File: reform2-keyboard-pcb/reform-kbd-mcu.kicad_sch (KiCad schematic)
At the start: 32 parts, among them J1 USB, J2 UART, J3 AUX, J4 Desktop USB, J6 AUX, SW83 RESET, SW84 SW_DIP_x01, U1 ATMEGA32U4-AU, U3 MCP1700-3302E_SOT23, Y1 16MHz

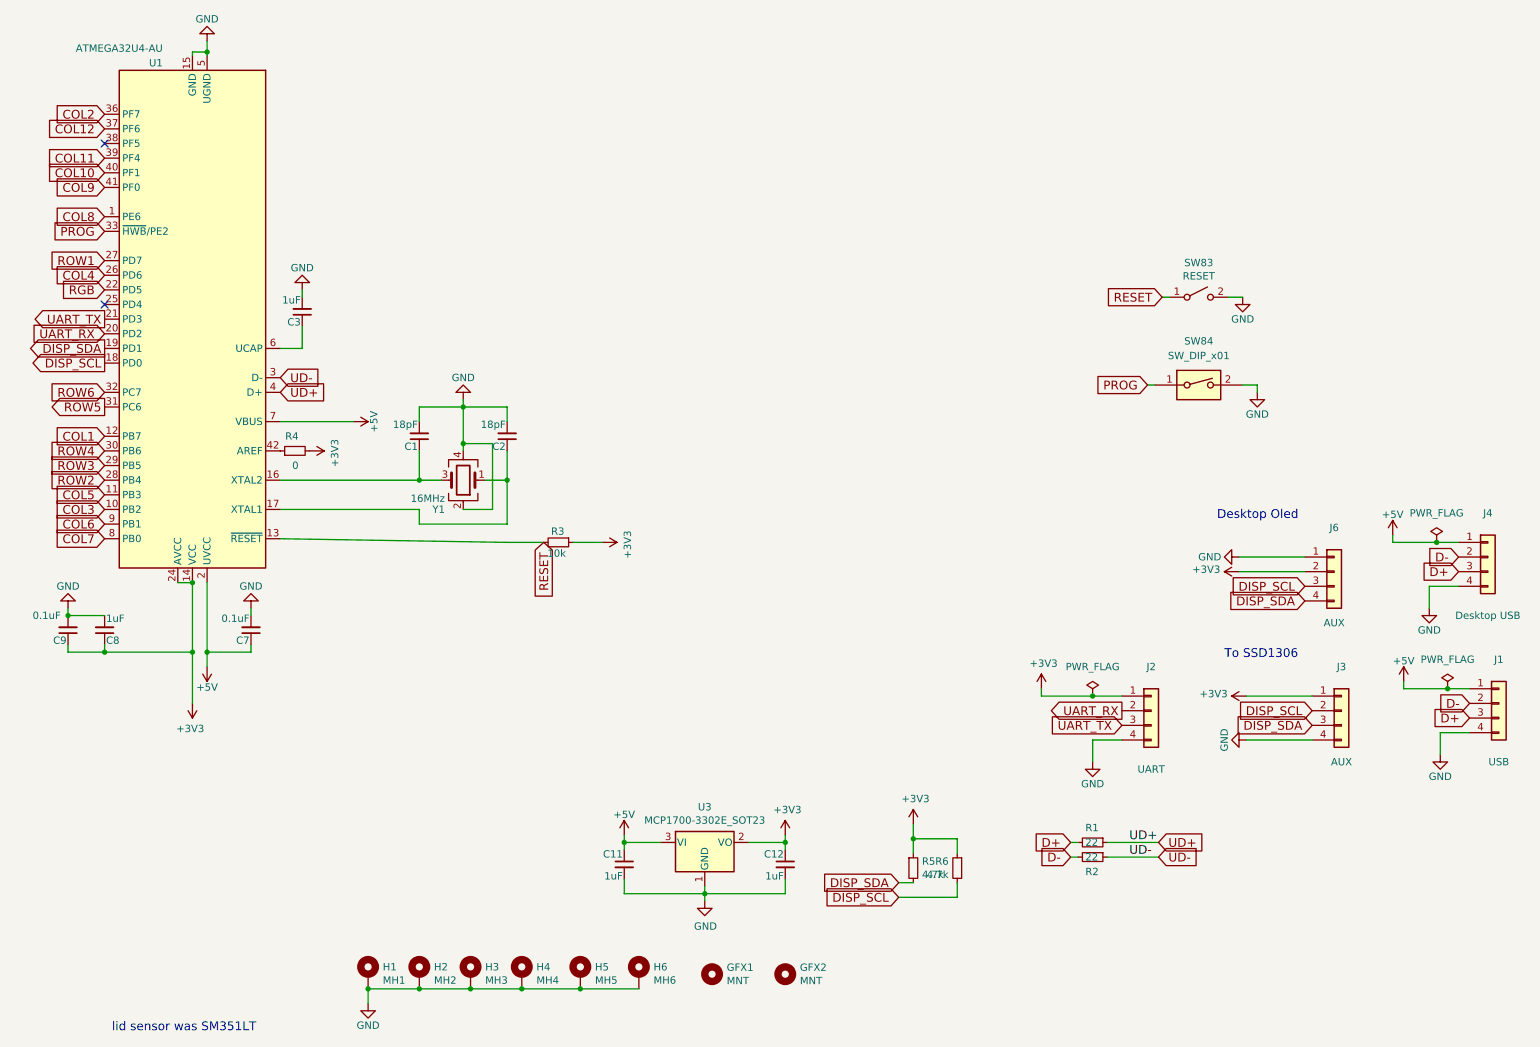
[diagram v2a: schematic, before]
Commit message: teensy2 w/ external 3volt regulator
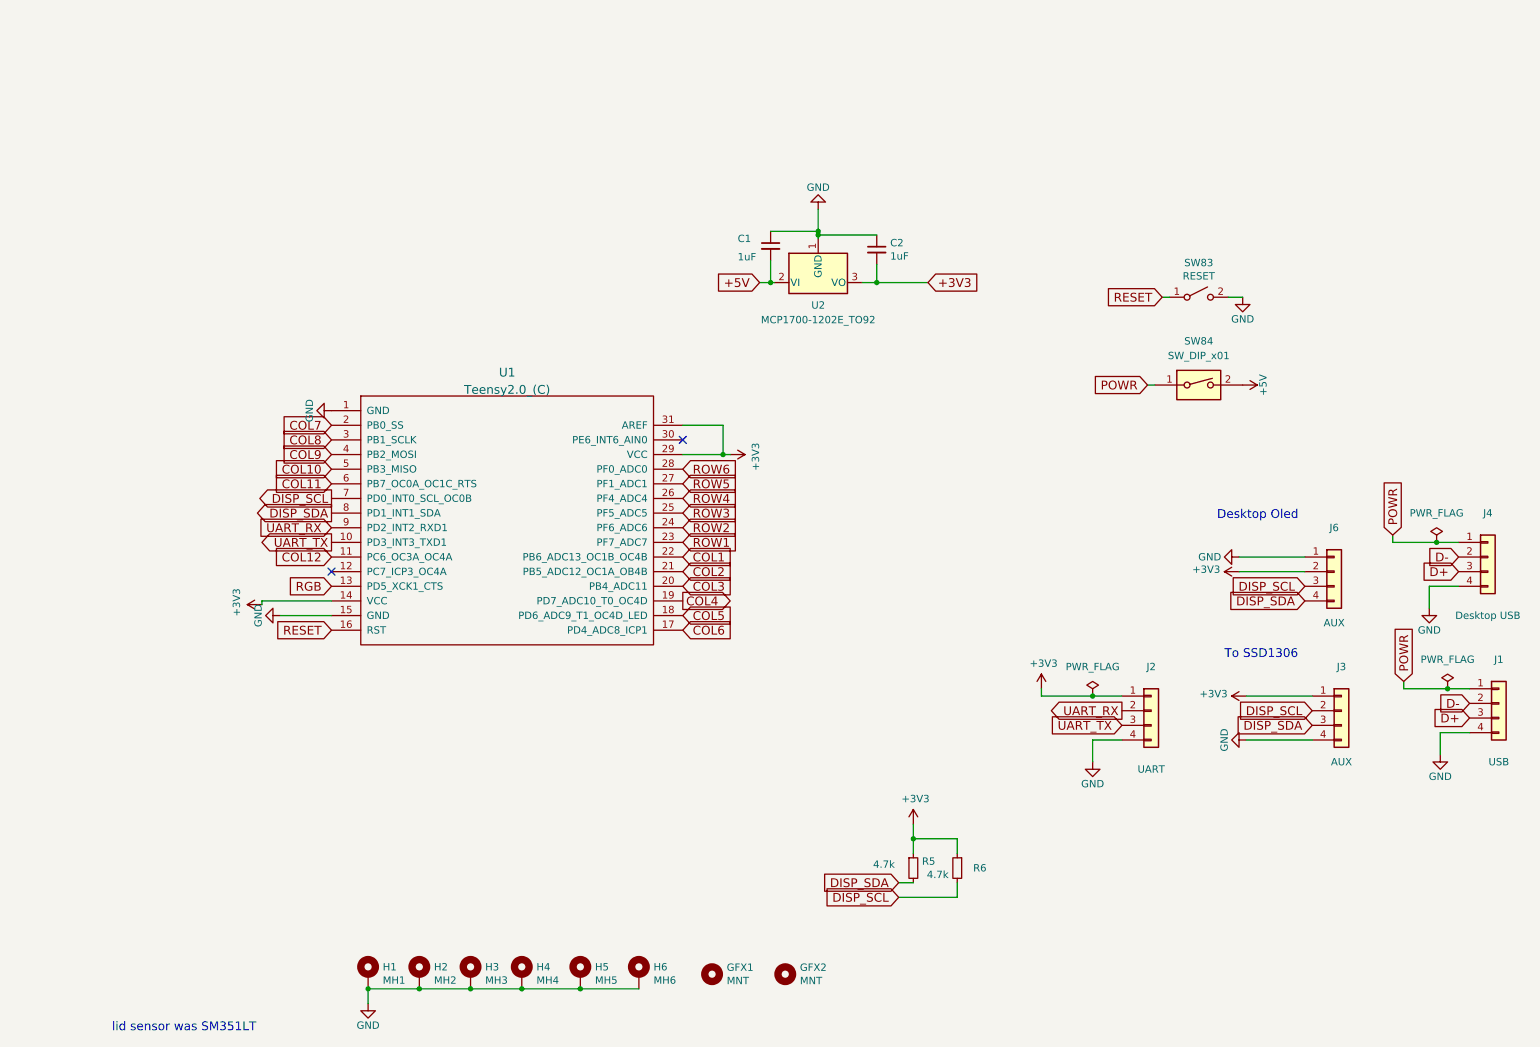
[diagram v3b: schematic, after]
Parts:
- removed C11, C12, C3, C8: 1uF, Capacitor_SMD:C_0805_2012Metric_Pad1.18x1.45mm_HandSolder, symbol reform2-keyboard-rescue:C_Small-Device
- removed C7, C9: 0.1uF, Capacitor_SMD:C_0805_2012Metric_Pad1.18x1.45mm_HandSolder, symbol reform2-keyboard-rescue:C_Small-Device
- removed R1, R2: 22, Resistor_SMD:R_0805_2012Metric_Pad1.20x1.40mm_HandSolder, symbol reform2-keyboard-rescue:R_Small-Device
- removed R3: 10k, Resistor_SMD:R_0805_2012Metric_Pad1.20x1.40mm_HandSolder, symbol reform2-keyboard-rescue:R_Small-Device
- removed R4: 0, Resistor_SMD:R_0805_2012Metric_Pad1.20x1.40mm_HandSolder, symbol reform2-keyboard-rescue:R_Small-Device
- removed U1: ATMEGA32U4-AU, Package_QFP:TQFP-44_10x10mm_P0.8mm, symbol reform2-keyboard-rescue:ATmega32U4-AU-MCU_Microchip_ATmega
- removed U3: MCP1700-3302E_SOT23, Package_TO_SOT_SMD:SOT-23, symbol reform2-keyboard-rescue:MCP1700-3302E_SOT23-Regulator_Linear
- removed Y1: 16MHz, Crystal:Crystal_SMD_3225-4Pin_3.2x2.5mm_HandSoldering, symbol reform2-keyboard-rescue:Crystal_GND24-Device
- added U1: Teensy2.0_(C), teensy:Teensy2.0, symbol teensy:Teensy2.0_(C)
- added U2: MCP1700-1202E_TO92, Package_TO_SOT_THT:TO-92_Inline, symbol Regulator_Linear:MCP1700-1202E_TO92
- C1, C2: value 18pF -> 1uF; Manufacturer Yageo -> Taiyo Yuden; Manufacturer_No CC0603JRNPO9BN180 -> JMK107BB7475KA-T
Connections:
- net +3V3: now also C2.2, U1.14 (VCC), U1.29 (VCC), U1.31 (AREF), U2.3 (VO)
- net +5V: now also C1.2, SW84.2, U2.2 (VI); no longer J1.1 (Pin_1), J4.1 (Pin_1)
- net COL1: now also U1.22 (PB6_ADC13_OC1B_OC4B)
- net COL10: now also U1.5 (PB3_MISO)
- net COL11: now also U1.6 (PB7_OC0A_OC1C_RTS)
- net COL12: now also U1.11 (PC6_OC3A_OC4A)
- net COL2: now also U1.21 (PB5_ADC12_OC1A_OB4B)
- net COL3: now also U1.20 (PB4_ADC11)
- net COL4: now also U1.19 (PD7_ADC10_T0_OC4D)
- net COL5: now also U1.18 (PD6_ADC9_T1_OC4D_LED)
- net COL6: now also U1.17 (PD4_ADC8_ICP1)
- net COL7: now also U1.2 (PB0_SS)
- net COL8: now also U1.3 (PB1_SCLK)
- net COL9: now also U1.4 (PB2_MOSI)
- net DISP_SCL: now also U1.7 (PD0_INT0_SCL_OC0B)
- net DISP_SDA: now also U1.8 (PD1_INT1_SDA)
- net GND: now also C1.1, C2.1, U1.1 (GND), U1.15 (GND), U2.1 (GND); no longer C1.2, C2.2, SW84.2
- net RESET: now also U1.16 (RST)
- net RGB: now also U1.13 (PD5_XCK1_CTS)
- net ROW1: now also U1.23 (PF7_ADC7)
- net ROW2: now also U1.24 (PF6_ADC6)
- net ROW3: now also U1.25 (PF5_ADC5)
- net ROW4: now also U1.26 (PF4_ADC4)
- net ROW5: now also U1.27 (PF1_ADC1)
- net ROW6: now also U1.28 (PF0_ADC0)
- net UART_RX: now also U1.9 (PD2_INT2_RXD1)
- net UART_TX: now also U1.10 (PD3_INT3_TXD1)
- net PROG renamed POWR
- net POWR: now also J1.1 (Pin_1), J4.1 (Pin_1)

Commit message: initial itsybitsy. Moved USB airwire & lcd locations
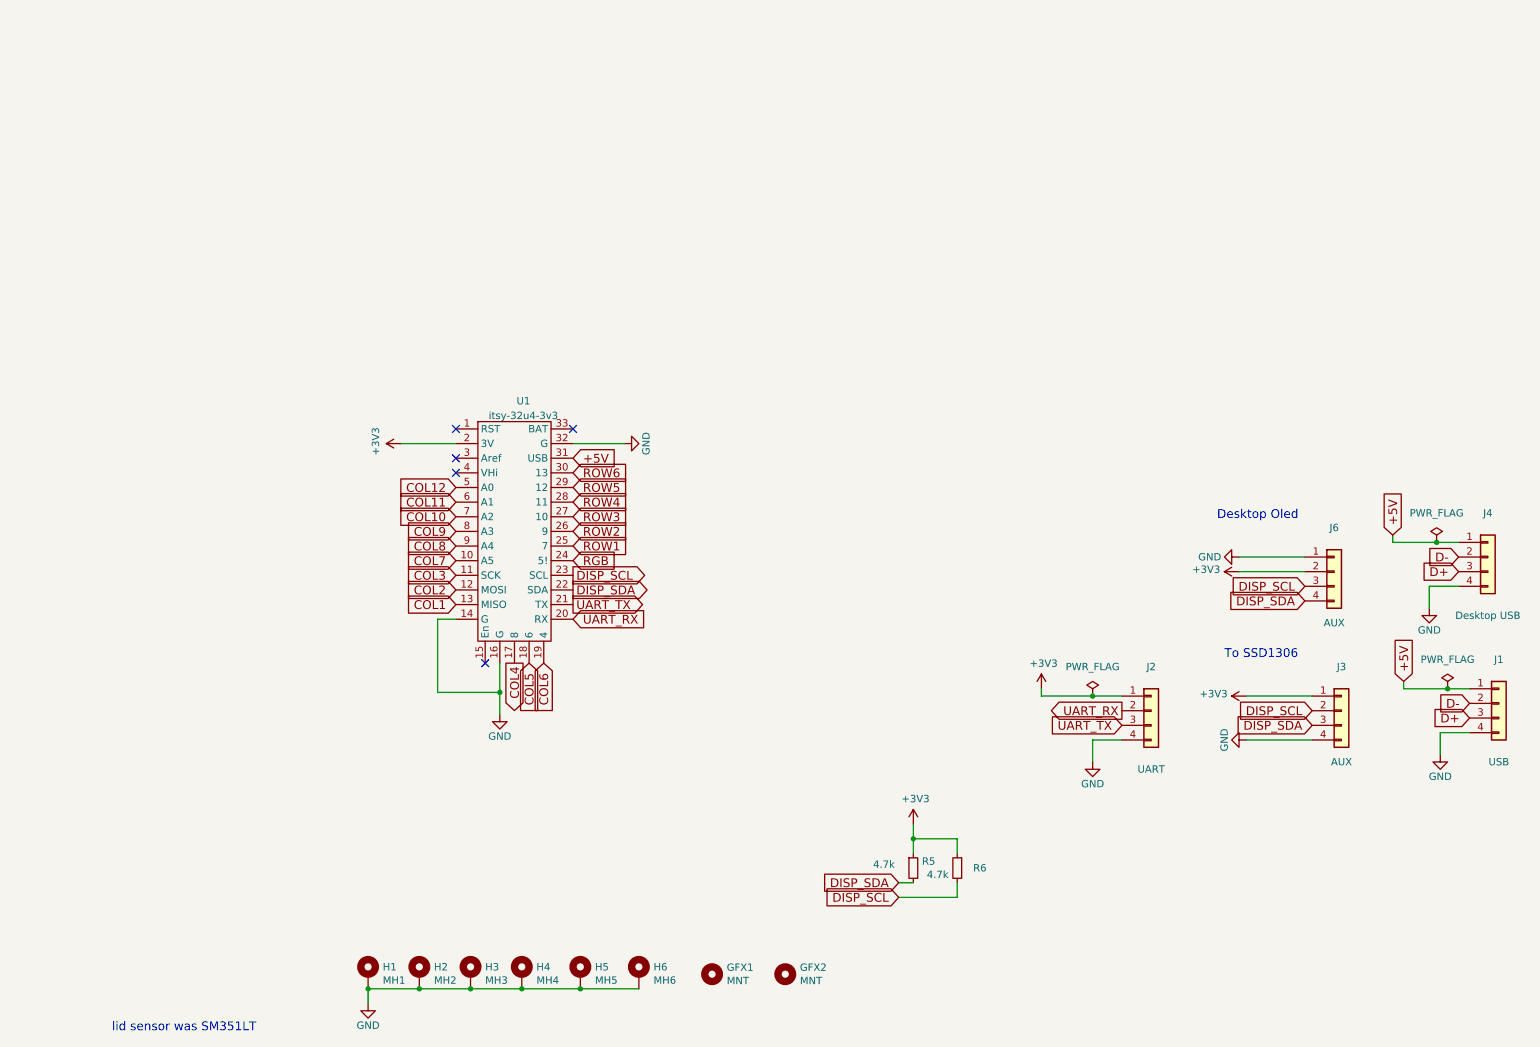
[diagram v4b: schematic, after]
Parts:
- removed C1, C2: 1uF, Capacitor_SMD:C_0805_2012Metric_Pad1.18x1.45mm_HandSolder, symbol reform2-keyboard-rescue:C_Small-Device
- removed SW83: RESET, Button_Switch_SMD:SW_Push_1P1T_NO_CK_KMR2, symbol reform2-keyboard-rescue:SW_SPST-Switch
- removed SW84: SW_DIP_x01, Button_Switch_SMD:SW_DIP_SPSTx01_Slide_Omron_A6S-110x_W8.9mm_P2.54mm, symbol reform2-keyboard-rescue:SW_DIP_x01-Switch
- removed U1: Teensy2.0_(C), teensy:Teensy2.0, symbol teensy:Teensy2.0_(C)
- removed U2: MCP1700-1202E_TO92, Package_TO_SOT_THT:TO-92_Inline, symbol Regulator_Linear:MCP1700-1202E_TO92
- added U1: itsy-32u4-3v3, Itsybitsy32u4:ItsyBitsy-32u4, symbol itsybitsy32u4:itsy-32u4-3v3
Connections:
- net POWR is gone; now on net +5V: J1.1 (Pin_1), J4.1 (Pin_1)
- net +3V3: now also U1.2 (3V)
- net +5V: now also U1.31 (USB)
- net COL1: now also U1.13 (MISO)
- net COL10: now also U1.7 (A2)
- net COL11: now also U1.6 (A1)
- net COL12: now also U1.5 (A0)
- net COL2: now also U1.12 (MOSI)
- net COL3: now also U1.11 (SCK)
- net COL4: now also U1.17 (8)
- net COL5: now also U1.18 (6)
- net COL6: now also U1.19 (4)
- net COL7: now also U1.10 (A5)
- net COL8: now also U1.9 (A4)
- net COL9: now also U1.8 (A3)
- net DISP_SCL: now also U1.23 (SCL)
- net DISP_SDA: now also U1.22 (SDA)
- net GND: now also U1.14 (G), U1.16 (G), U1.32 (G)
- net RGB: now also U1.24 (5!)
- net ROW1: now also U1.25 (7)
- net ROW2: now also U1.26 (9)
- net ROW3: now also U1.27 (10)
- net ROW4: now also U1.28 (11)
- net ROW5: now also U1.29 (12)
- net ROW6: now also U1.30 (13)
- net UART_RX: now also U1.20 (RX)
- net UART_TX: now also U1.21 (TX)
- no-connect marks 2 -> 5

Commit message: added testpoints for RGB, fixed diode directions, started BOM & top POS for assembly
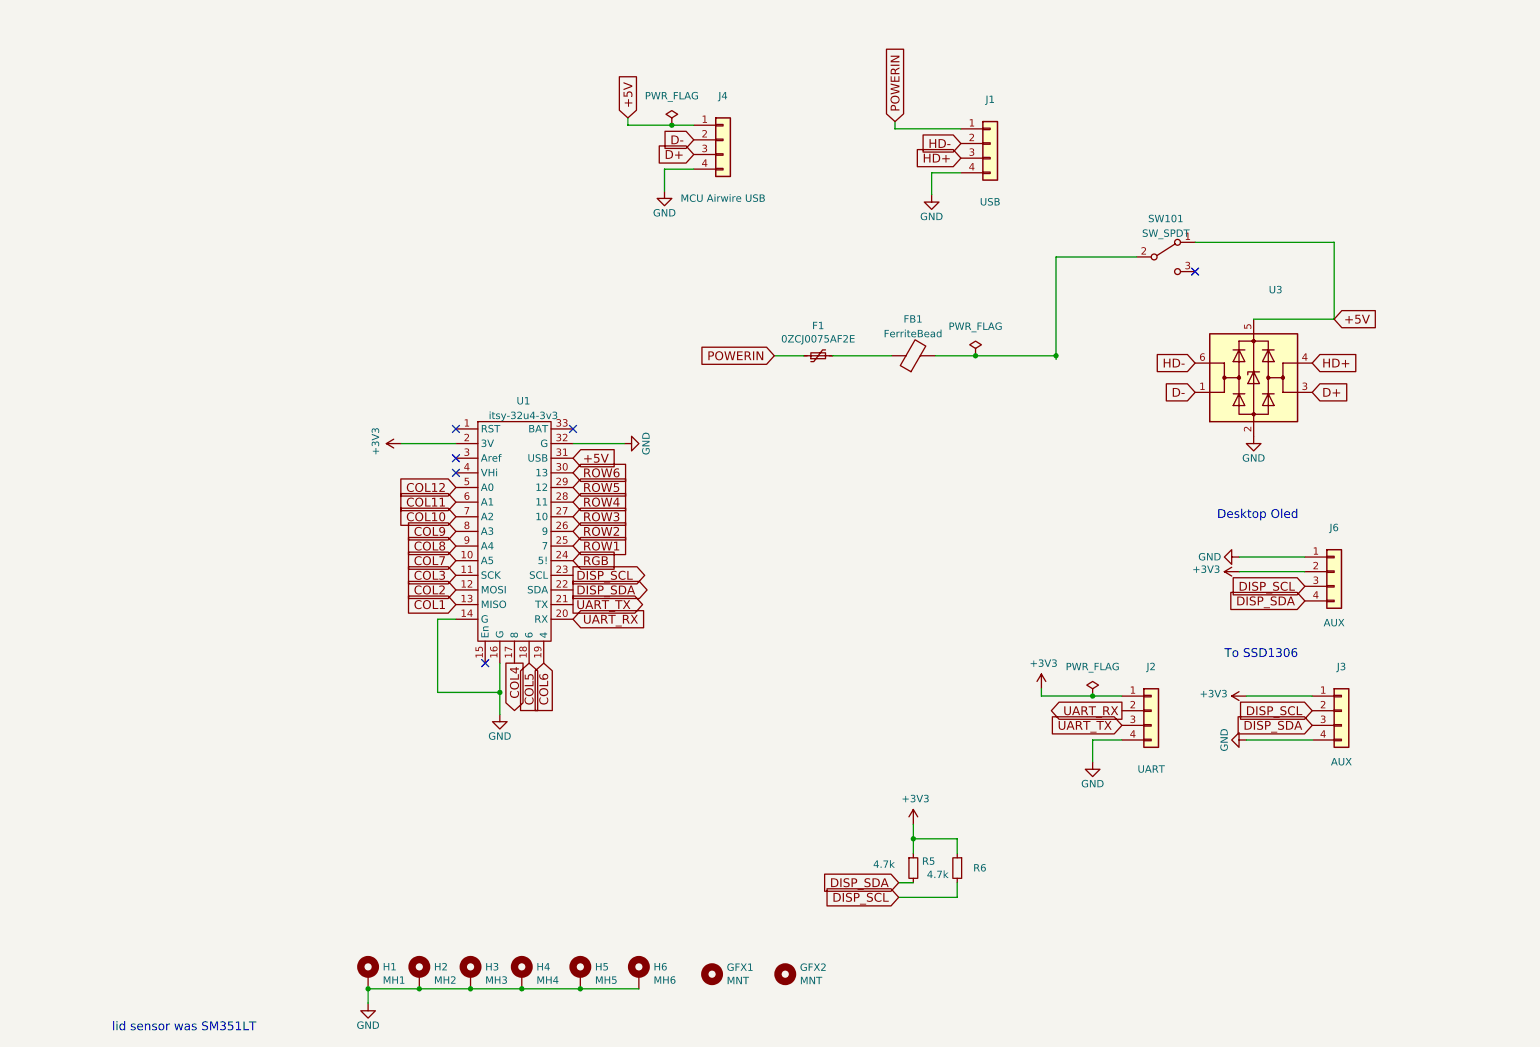
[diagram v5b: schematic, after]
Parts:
- added F1: 0ZCJ0075AF2E, Resistor_SMD:R_1206_3216Metric, symbol Device:Polyfuse_Small
- added FB1: FerriteBead, Resistor_SMD:R_0805_2012Metric_Pad1.20x1.40mm_HandSolder, symbol Device:FerriteBead
- added SW101: SW_SPDT, Button_Switch_THT:SW_Push_1P2T_Vertical_E-Switch_800UDP8P1A1M6, symbol Switch:SW_SPDT
- added U3: ~, Package_TO_SOT_SMD:SOT-23-6_Handsoldering, symbol Power_Protection:USBLC6-2SC6
- J4: value Desktop USB -> MCU Airwire USB; footprint Connector_PinHeader_2.54mm:PinHeader_1x04_P2.54mm_Horizontal -> Connector_PinHeader_2.54mm:PinHeader_1x04_P2.54mm_Vertical
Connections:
- net +5V: now also SW101.1 (A), U3.5 (VBUS); no longer J1.1 (Pin_1)
- net D+: now also U3.3 (I/O2); no longer J1.3 (Pin_3)
- net D-: now also U3.1 (I/O1); no longer J1.2 (Pin_2)
- net GND: now also U3.2 (GND)
- new net: FB1.2, SW101.2 (B)
- new net: F1.2, FB1.1
- new net HD+: J1.3 (Pin_3), U3.4 (I/O2)
- new net HD-: J1.2 (Pin_2), U3.6 (I/O1)
- new net POWERIN: F1.1, J1.1 (Pin_1)
- no-connect marks 5 -> 6
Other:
- moved on the sheet: J1, J4

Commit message: improve docs
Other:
- note added: "B1"
- note added: "B2"
- note added: "B3"
- note added: "B4"
- note added: "B5"
- note added: "B6"
- note added: "B7"
- note added: "C7"
- note added: "D0"
- note added: "D1"
- note added: "D2"
- note added: "D3"
- note added: "D4"
- note added: "D6"
- note added: "D7"
- note added: "E6"
- note added: "F0"
- note added: "F1"
- note added: "F4"
- note added: "F5"
- note added: "F6"
- note added: "F7"
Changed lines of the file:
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@@
     (stroke (width 0) (type default) (color 0 0 0 0))
   )
+  (text "B4" (at 96.52 140.335 90)
+    (effects (font (size 1.524 1.524)) (justify left bottom))
+  )
+  (text "D6" (at 116.205 96.52 0)
+    (effects (font (size 1.524 1.524)) (justify left bottom))
+  )
+  (text "F1" (at 70.485 107.315 0)
+    (effects (font (size 1.524 1.524)) (justify left bottom))
+  )
+  (text "E6" (at 114.935 107.315 0)
+    (effects (font (size 1.524 1.524)) (justify left bottom))
+  )
+  (text "B7" (at 115.57 99.695 0)
+    (effects (font (size 1.524 1.524)) (justify left bottom))
+  )
+  (text "D3" (at 119.38 117.475 0)
+    (effects (font (size 1.524 1.524)) (justify left bottom))
+  )
+  (text "C7" (at 114.935 109.855 0)
+    (effects (font (size 1.524 1.524)) (justify left bottom))
+  )
+  (text "D0" (at 120.015 111.76 0)
+    (effects (font (size 1.524 1.524)) (justify left bottom))
+  )
+  (text "B5" (at 114.935 104.775 0)
+    (effects (font (size 1.524 1.524)) (justify left bottom))
+  )
+  (text "F5" (at 70.485 102.235 0)
+    (effects (font (size 1.524 1.524)) (justify left bottom))
+  )
   (text "To SSD1306" (at 218.44 125.73 0)
+    (effects (font (size 1.524 1.524)) (justify left bottom))
+  )
+  (text "F6" (at 70.485 99.695 0)
+    (effects (font (size 1.524 1.524)) (justify left bottom))
+  )
+  (text "D7" (at 99.06 140.335 90)
+    (effects (font (size 1.524 1.524)) (justify left bottom))
+  )
+  (text "F0" (at 70.485 109.855 0)
+    (effects (font (size 1.524 1.524)) (justify left bottom))
+  )
+  (text "F7" (at 70.485 97.155 0)
+    (effects (font (size 1.524 1.524)) (justify left bottom))
+  )
+  (text "C7" (at 116.205 93.98 0)
+    (effects (font (size 1.524 1.524)) (justify left bottom))
+  )
+  (text "F4" (at 70.485 104.775 0)
+    (effects (font (size 1.524 1.524)) (justify left bottom))
+  )
+  (text "B2" (at 70.485 114.935 0)
+    (effects (font (size 1.524 1.524)) (justify left bottom))
+  )
+  (text "B6" (at 115.57 102.235 0)
     (effects (font (size 1.524 1.524)) (justify left bottom))
   )
@@
     (effects (font (size 1.524 1.524)) (justify left bottom))
   )
+  (text "B1" (at 70.485 112.395 0)
+    (effects (font (size 1.524 1.524)) (justify left bottom))
+  )
+  (text "D2" (at 119.38 120.015 0)
+    (effects (font (size 1.524 1.524)) (justify left bottom))
+  )
+  (text "B3" (at 70.485 117.475 0)
+    (effects (font (size 1.524 1.524)) (justify left bottom))
+  )
+  (text "D4" (at 101.6 140.335 90)
+    (effects (font (size 1.524 1.524)) (justify left bottom))
+  )
+  (text "D1" (at 119.38 114.935 0)
+    (effects (font (size 1.524 1.524)) (justify left bottom))
+  )
